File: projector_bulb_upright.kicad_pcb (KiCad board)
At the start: 2 copper layers, 38.1 x 76.2 mm, 17 parts, among them U1 AL8860, U2 L7815

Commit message: Revision 2, still needs documentation and things
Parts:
- removed JP2: Jumper_2_Bridged, Jumper:SolderJumper-2_P1.3mm_Bridged_RoundedPad1.0x1.5mm
- added JP1: Jumper_2_Bridged, Jumper:SolderJumper-2_P1.3mm_Bridged_RoundedPad1.0x1.5mm, F.Cu at (140.7, 15.4)
- C5: value 4.7u -> 22u
- R2: value 51k -> 7.5k
- U1: value AL8860 -> PAM2863; footprint Package_TO_SOT_SMD:TSOT-23-5_HandSoldering -> Package_SO:HTSOP-8-1EP_3.9x4.9mm_P1.27mm_EP2.4x3.2mm
- U2: value L7815 -> AP7381-33Y; footprint Package_TO_SOT_SMD:TO-263-2 -> Package_TO_SOT_SMD:SOT-89-3
- moved C5 11.0 mm to (117.3, 57.7), turned to 90 degrees
- moved D2 9.27 mm to (111.8, 45.7), turned to 90 degrees
- moved U1 6.40 mm to (112.8, 57.6), turned to 270 degrees
- moved R1 4.81 mm to (118.4, 50.3), turned to 180 degrees
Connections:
- C5 pad 1: Net-(C5-Pad1) -> GND_UPRIGHT
- C5 pad 2: Net-(C5-Pad2) -> VIN_UPRIGHT
- D2 pad 1: Net-(C5-Pad1) -> VIN_UPRIGHT
- R1 pad 1: Net-(C5-Pad1) -> VIN_UPRIGHT
- R2 pad 1: Net-(C5-Pad1) -> Net-(R2-Pad1)
- REF** pad 1: Net-(C5-Pad2) -> GND_UPRIGHT (x2)
- REF** pad 1: Net-(J5-Pad1) -> VIN_UPRIGHT (x2)
- RV1 pad 1: Net-(C5-Pad2) -> Net-(R2-Pad1)
- RV1 pad 3: Net-(R2-Pad2) -> GND_UPRIGHT
- U1 pad 1: Net-(D2-Pad2) -> VIN_UPRIGHT
- U1 pad 2: Net-(C5-Pad2) -> Net-(J8-Pad1)
- U1 pad 3: Net-(JP2-Pad1) -> GND_UPRIGHT
- U1 pad 4: Net-(J8-Pad1) -> DIMMING
- U1 pad 5: Net-(C5-Pad1) -> Net-(D2-Pad2)
- U2 pad 1: Net-(J5-Pad1) -> Net-(R2-Pad2)
- U2 pad 2: Net-(C5-Pad2) -> GND_UPRIGHT
- U2 pad 3: Net-(C5-Pad1) -> VIN_UPRIGHT
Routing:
- net GND_UPRIGHT: track 0.00 -> 125.3 mm, vias 0 -> 2
- net Net-(C5-Pad2): track 111.7 -> 0.00 mm, vias 11 -> 0
- net Net-(C5-Pad1): track 105.2 -> 0.00 mm, vias 2 -> 0
- net VIN_UPRIGHT: track 0.00 -> 77.7 mm, vias 0 -> 1
- net DIMMING: track 0.00 -> 67.0 mm, vias 0 -> 2
- net Net-(R2-Pad2): track 6.84 -> 67.8 mm, vias 0 -> 2
- net Net-(JP1-Pad1): track 53.4 -> 5.39 mm
- net Net-(J5-Pad1): track 22.0 -> 0.00 mm, vias 1 -> 0
- net Net-(JP2-Pad1): track 17.9 -> 0.00 mm, vias 1 -> 0
- net Net-(J8-Pad1): track 53.1 -> 44.0 mm, vias 2 -> 8
- net Net-(R2-Pad1): track 0.00 -> 9.05 mm
- net Net-(J7-Pad1): track 29.1 -> 22.5 mm, vias 1 -> 7
- net Net-(D2-Pad2): track 49.4 -> 50.6 mm
- removed copper zone on B.Cu, net Net-(C5-Pad2)
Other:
- board text added: "LED DCA Lamp Revision 2 April 2021"
- board text added: "LED front on this side"
- board text added: "ettingersam@gmail.com"

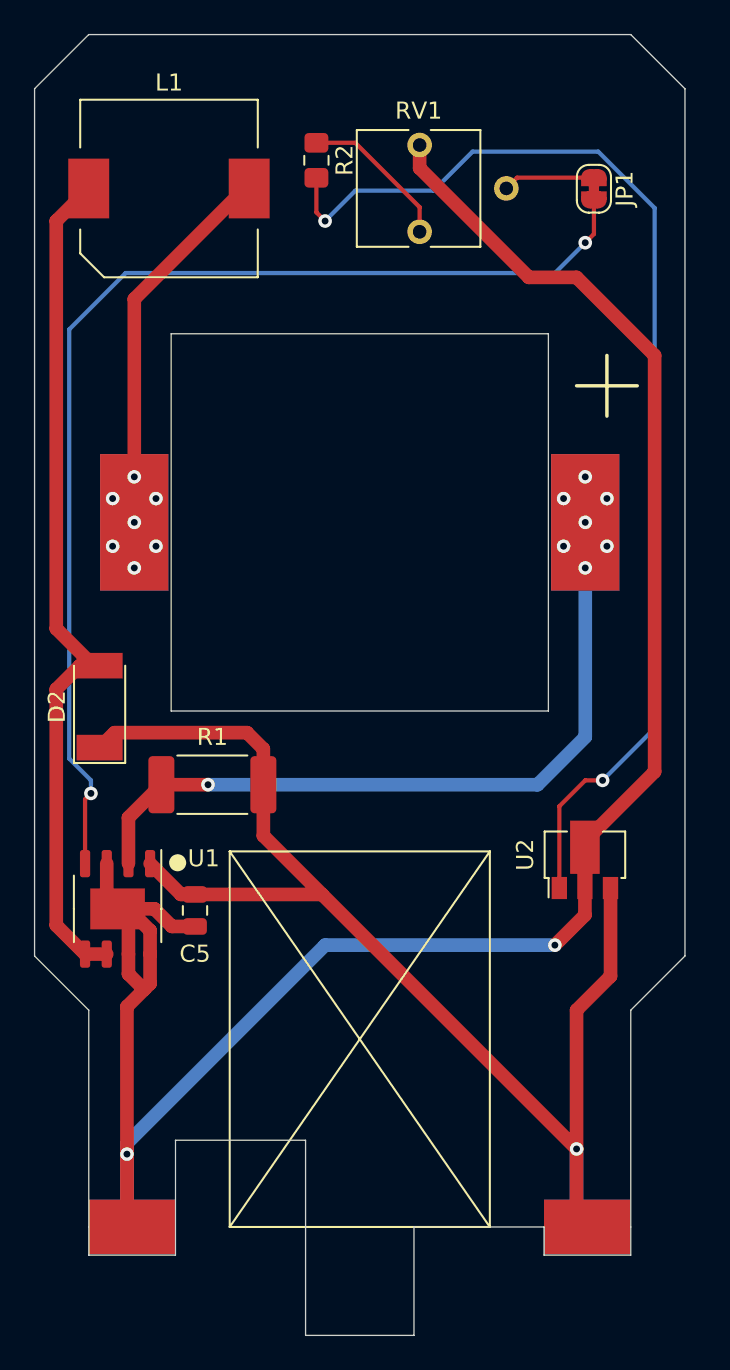
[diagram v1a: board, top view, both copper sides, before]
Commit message: Much progress on Aluminum PCB
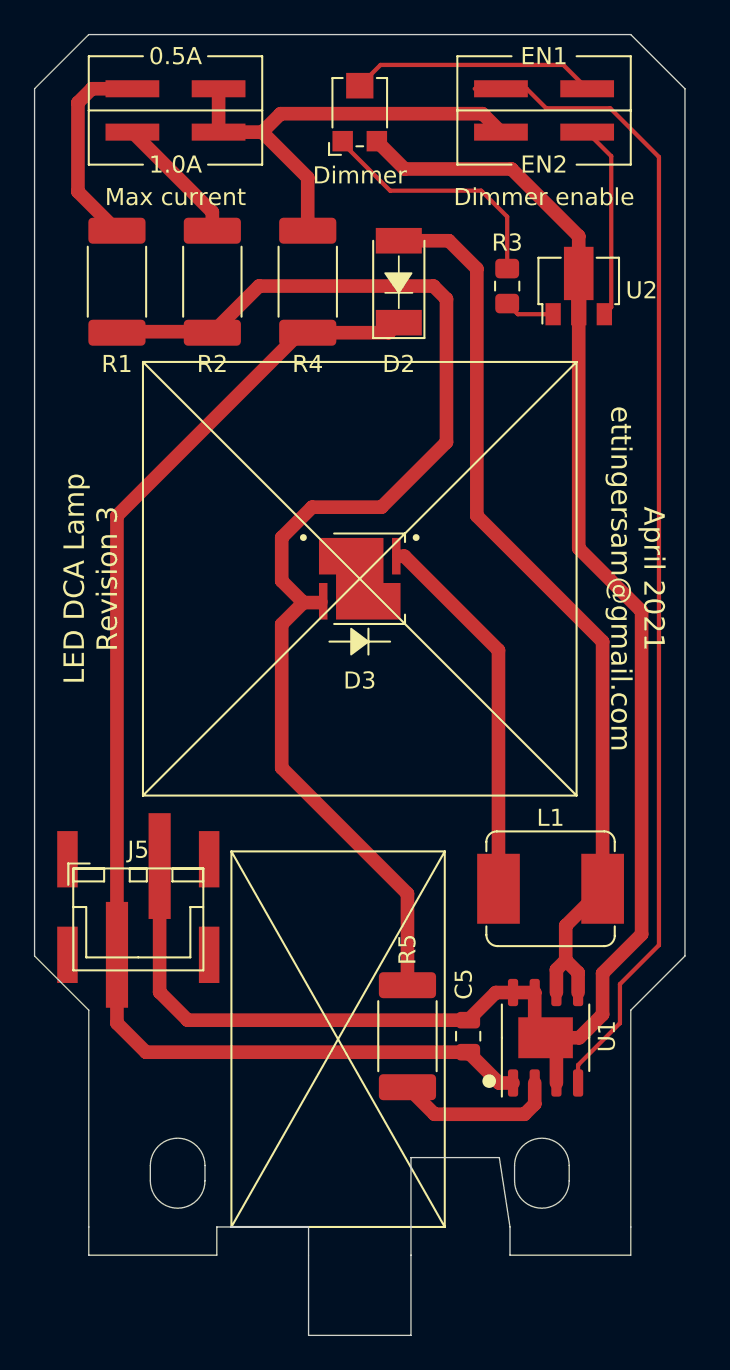
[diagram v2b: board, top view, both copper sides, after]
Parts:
- removed JP1: Jumper_2_Bridged, Jumper:SolderJumper-2_P1.3mm_Bridged_RoundedPad1.0x1.5mm
- removed REF** (x8): angle_joint, projector_bulb:angle_joint
- added D3: LED_Small_ALT, LED_SMD:LED_Cree-XHP50_12V, F.Cu at (127.0, 38.2)
- added J5: to_base, projector_bulb:JST_XA_1x02_P2.50mm_SMD, F.Cu at (112.8, 57.7)
- added J7: Conn_02x02_Odd_Even, Connector_PinHeader_2.54mm:PinHeader_2x02_P2.54mm_Vertical_SMD, F.Cu at (116.2, 10.8)
- added J8: Conn_02x02_Odd_Even, Connector_PinHeader_2.54mm:PinHeader_2x02_P2.54mm_Vertical_SMD, F.Cu at (137.8, 10.8)
- added R2: 0.200, Resistor_SMD:R_2512_6332Metric_Pad1.52x3.35mm_HandSolder, F.Cu at (118.4, 20.8)
- added R4: 0Ω, Resistor_SMD:R_2512_6332Metric_Pad1.52x3.35mm_HandSolder, F.Cu at (124.0, 20.8)
- added R5: 0Ω, Resistor_SMD:R_2512_6332Metric_Pad1.52x3.35mm_HandSolder, F.Cu at (129.8, 65.0)
- L1: footprint projector_bulb:L_Wuerth_WE-PD-100100 -> projector_bulb:L_KEMET_MPLCV_0654_7.9x6.5mm
- RV1: footprint Potentiometer_THT:Potentiometer_Vishay_T73YP_Vertical -> Potentiometer_SMD:Potentiometer_Bourns_TC33X_Vertical
- moved L1 46.7 mm to (138.2, 56.4)
- moved U2 33.6 mm to (139.8, 21.1)
- moved D2 30.4 mm to (129.3, 20.8)
- moved R1 30.0 mm to (112.8, 20.8), turned to 270 degrees
- moved U1 26.2 mm to (137.9, 65.1), turned to 90 degrees
- moved C5 17.6 mm to (133.3, 65.0), turned to 270 degrees
- moved R3 13.4 mm to (135.6, 21.1)
- moved RV1 7.92 mm to (127.0, 10.8), turned to 90 degrees
- renumbered R2 to R3
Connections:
- L1 pad 1: Net-(D2-Pad2) -> Net-(D3-Pad1)
- L1 pad 2: Net-(J7-Pad1) -> Net-(D2-Pad2)
- R1 pad 1: VIN_UPRIGHT -> Net-(J7-Pad1)
- R1 pad 2: Net-(J8-Pad1) -> CURRENT_SELECT
- U1 pad 2: Net-(J8-Pad1) -> Net-(R5-Pad2)
- U2 pad 3: VIN_UPRIGHT -> Net-(J8-Pad4)
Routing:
- net CURRENT_SELECT: track 0.00 -> 72.6 mm
- net Net-(R3-Pad2): track 67.8 -> 2.95 mm, vias 2 -> 0
- net Net-(J8-Pad1): track 44.0 -> 0.00 mm, vias 8 -> 0
- net VIN_NET_TIE: track 0.00 -> 26.9 mm
- net GND_UPRIGHT: track 125.3 -> 102.6 mm, vias 2 -> 0
- net Net-(D3-Pad1): track 0.00 -> 22.1 mm
- net Net-(J8-Pad4): track 0.00 -> 11.4 mm
- net Net-(J7-Pad1): track 22.5 -> 12.0 mm, vias 7 -> 0
- net Net-(R5-Pad2): track 0.00 -> 9.59 mm
- net Net-(J8-Pad2): track 5.39 -> 14.4 mm
- net Net-(J7-Pad3): track 0.00 -> 7.72 mm
- net Net-(R3-Pad1): track 9.05 -> 14.6 mm
- net Net-(D2-Pad2): track 50.6 -> 54.7 mm
- net DIMMING: track 67.0 -> 68.7 mm, vias 2 -> 0
- net VIN_UPRIGHT: track 77.7 -> 76.4 mm, vias 1 -> 0
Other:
- outline, holes or cut-outs redrawn
- board text added: "0.5A"
- board text added: "1.0A"
- board text added: "April 2021 ettingersam@gmail.com"
- board text added: "Dimmer"
- board text added: "Dimmer enable"
- board text added: "EN1"
- board text added: "EN2"
- board text added: "LED DCA Lamp Revision 3"
- board text added: "Max current"
- board text removed: "LED DCA Lamp Revision 2 April 2021"
- board text removed: "LED front on this side"
- board text removed: "ettingersam@gmail.com"

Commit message: Add test points, replaced some expensive components with cheaper alternatives
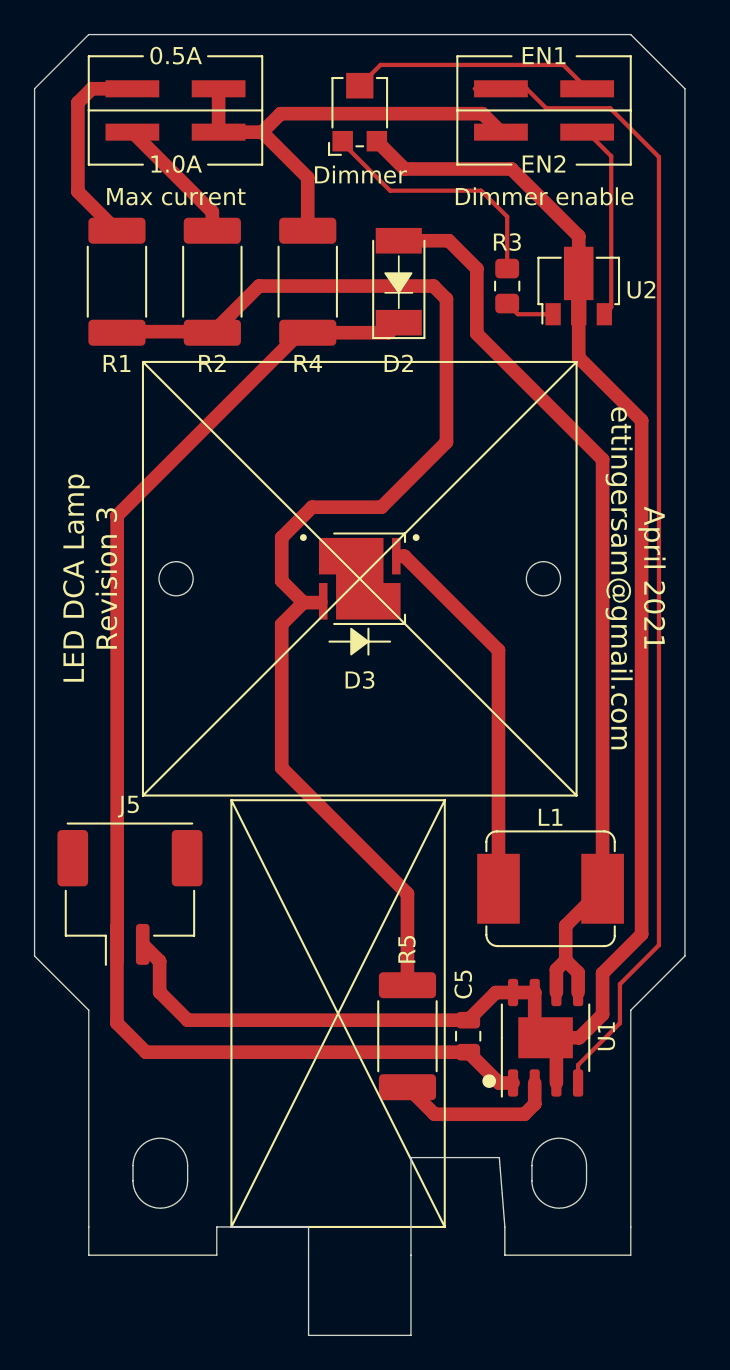
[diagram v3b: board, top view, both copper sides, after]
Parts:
- added HS1: Heatsink, projector_bulb:Heatsink_35x35x18mm, B.Cu at (127.0, 33.0)
- added LENS1: Lens, projector_bulb:LENS_LEDIL_CA16370_HB-SQ-W, F.Cu at (127.0, 38.2)
- J5: footprint projector_bulb:JST_XA_1x02_P2.50mm_SMD -> Connector_Molex:Molex_CLIK-Mate_505405-0270_1x02-1MP_P1.50mm_Vertical
- moved J5 1.08 mm to (113.5, 56.9)
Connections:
- net CURRENT_SELECT renamed Net-(D3-Pad2)
- net VIN_NET_TIE renamed Net-(J7-Pad2)
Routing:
- net GND_UPRIGHT: track 102.6 -> 98.5 mm
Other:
- outline, holes or cut-outs redrawn

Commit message: BOM and readme updated
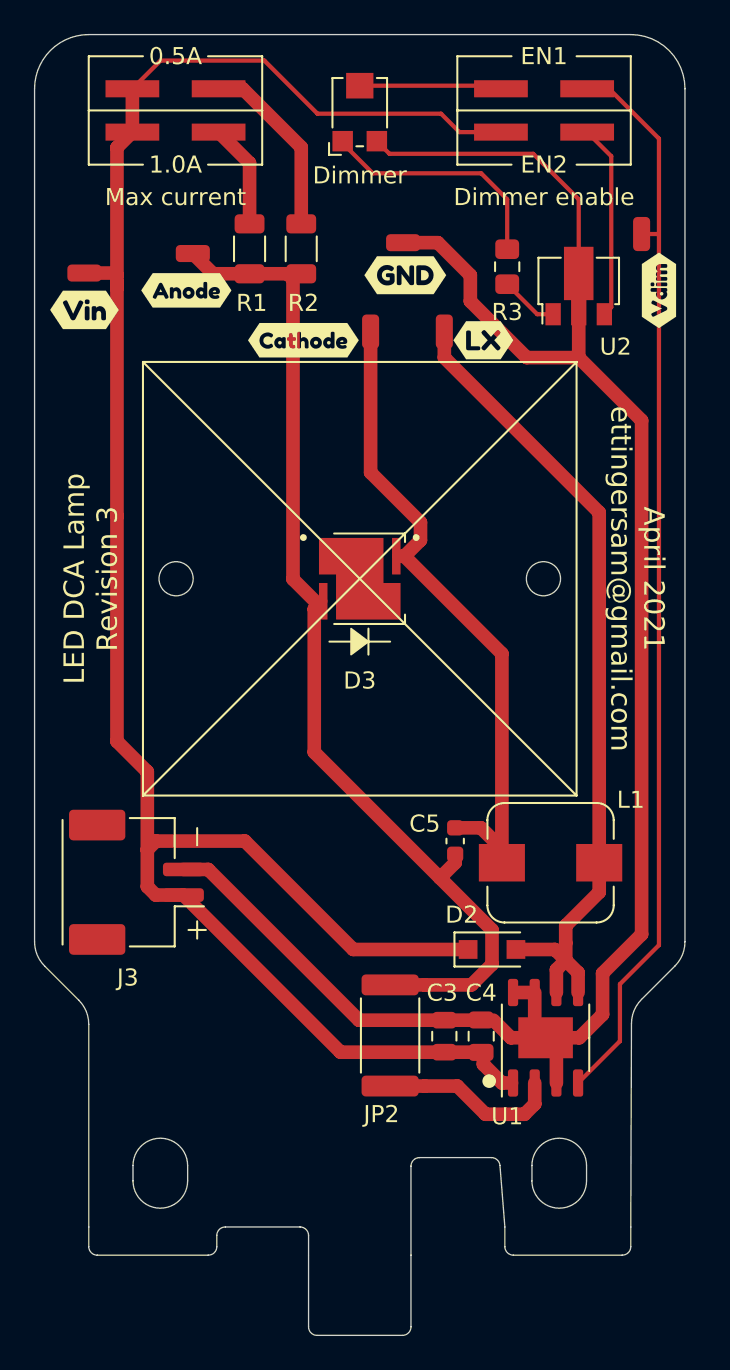
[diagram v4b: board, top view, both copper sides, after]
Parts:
- removed the J5 at (113.5, 56.9)
- removed R4, R5: 0Ω, Resistor_SMD:R_2512_6332Metric_Pad1.52x3.35mm_HandSolder
- added C4: 10μ, Capacitor_SMD:C_0805_2012Metric, F.Cu at (134.1, 65.0)
- added C5: 1μ, Capacitor_SMD:C_0603_1608Metric, F.Cu at (132.6, 53.6)
- added J3: to_base, Connector_Molex:Molex_CLIK-Mate_505405-0270_1x02-1MP_P1.50mm_Vertical, F.Cu at (113.9, 56.0)
- added JP2: Jumper_NC_Small, Resistor_SMD:R_2512_6332Metric, F.Cu at (128.8, 65.0)
- added TP1: TestPoint, projector_bulb:Test_Point_0603, F.Cu at (110.9, 20.3)
- added TP2: TestPoint, projector_bulb:Test_Point_0603, F.Cu at (129.5, 18.5)
- added TP3: TestPoint, projector_bulb:Test_Point_0603, F.Cu at (132.0, 23.7)
- added TP4: TestPoint, projector_bulb:Test_Point_0603, F.Cu at (143.5, 18.0)
- added TP5: TestPoint, projector_bulb:Test_Point_0603, F.Cu at (117.2, 19.2)
- added TP6: TestPoint, projector_bulb:Test_Point_0603, F.Cu at (127.6, 23.7)
- added svg2mod: G***, label, F.Cu at (134.2, 24.3)
- added svg2mod: G***, label, F.Cu at (116.8, 21.3)
- added svg2mod: G***, label, F.Cu at (110.9, 22.5)
- added svg2mod: G***, label, F.Cu at (129.7, 20.4)
- added svg2mod: G***, label, F.Cu at (144.5, 21.3)
- added svg2mod: G***, label, F.Cu at (123.7, 24.3)
- C3: renamed from C5; value 22u -> 10μ
- D2: value D_Schottky -> Schottky; footprint Diode_SMD:D_MELF -> Diode_SMD:D_SOD-123F
- D3: value LED_Small_ALT -> LED
- L1: value 47u -> 47μ; footprint projector_bulb:L_KEMET_MPLCV_0654_7.9x6.5mm -> projector_bulb:panasonic_PCC-M0748M
- R1: renamed from R2; footprint Resistor_SMD:R_2512_6332Metric_Pad1.52x3.35mm_HandSolder -> Resistor_SMD:R_1206_3216Metric
- R2: renamed from R1; footprint Resistor_SMD:R_2512_6332Metric_Pad1.52x3.35mm_HandSolder -> Resistor_SMD:R_1206_3216Metric
- moved D2 39.5 mm to (134.7, 59.9), turned to 0 degrees
- moved R2 11.0 mm to (123.6, 18.9)
- moved R1 2.91 mm to (120.5, 18.9)
- moved L1 1.52 mm to (138.2, 54.9)
- moved C3 1.40 mm to (132.0, 65.0)
- moved R3 1.13 mm to (135.6, 19.9)
- renumbered J7 to J4, J8 to J5
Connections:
- J4 pad 1: Net-(J7-Pad1) -> VIN_UPRIGHT
- J4 pad 2: Net-(J7-Pad2) -> Net-(J4-Pad2)
- J4 pad 3: Net-(J7-Pad3) -> VIN_UPRIGHT
- J4 pad 4: Net-(J7-Pad2) -> Net-(J4-Pad4)
- J5 pad 3: Net-(J7-Pad2) -> VIN_UPRIGHT
- R1 pad 1: Net-(J7-Pad3) -> Net-(J4-Pad4)
- R2 pad 1: Net-(J7-Pad1) -> Net-(J4-Pad2)
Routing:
- net VIN_UPRIGHT: track 76.4 -> 123.5 mm
- net Net-(J7-Pad2): track 26.9 -> 0.00 mm
- net Net-(C5-Pad1): track 22.1 -> 39.7 mm
- net GND_UPRIGHT: track 98.5 -> 112.9 mm
- net Net-(C5-Pad2): track 72.6 -> 60.0 mm
- net Net-(J7-Pad1): track 12.0 -> 0.00 mm
- net Net-(J4-Pad2): track 0.00 -> 10.7 mm
- net Net-(J7-Pad3): track 7.72 -> 0.00 mm
- net Net-(J5-Pad2): track 14.4 -> 8.09 mm
- net Net-(J4-Pad4): track 0.00 -> 6.12 mm
- net Net-(D2-Pad2): track 54.7 -> 48.9 mm
- net DIMMING: track 68.7 -> 63.7 mm
- net Net-(JP2-Pad1): track 9.59 -> 10.6 mm
- net Net-(R3-Pad1): track 14.6 -> 14.0 mm
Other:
- outline, holes or cut-outs redrawn
- net class Base Track added: clearance 0.25, trace_width 1, via_dia 0.8, via_drill 0.4
- rule pad_to_mask_clearance: 0.05 -> 0
